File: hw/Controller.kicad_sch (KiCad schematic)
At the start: 44 parts, among them J201 Conn_01x08, J202 Molex-105017-0001, J203 Conn_01x03, J204 Conn_01x02, J205 Conn_01x02, J206 Conn_01x02, J207 Conn_01x02, P201 Current-Probe, Q201 DTC114EE, U201 STM32F401XX-LQFP64, U202 TLV62150A, X201 Mounting-Hole-M3, X202 Mounting-Hole-M3, X203 Mounting-Hole-M3, X204 Mounting-Hole-M3, Y201 MCSJK-7I-8.00-18-30-60-B-30

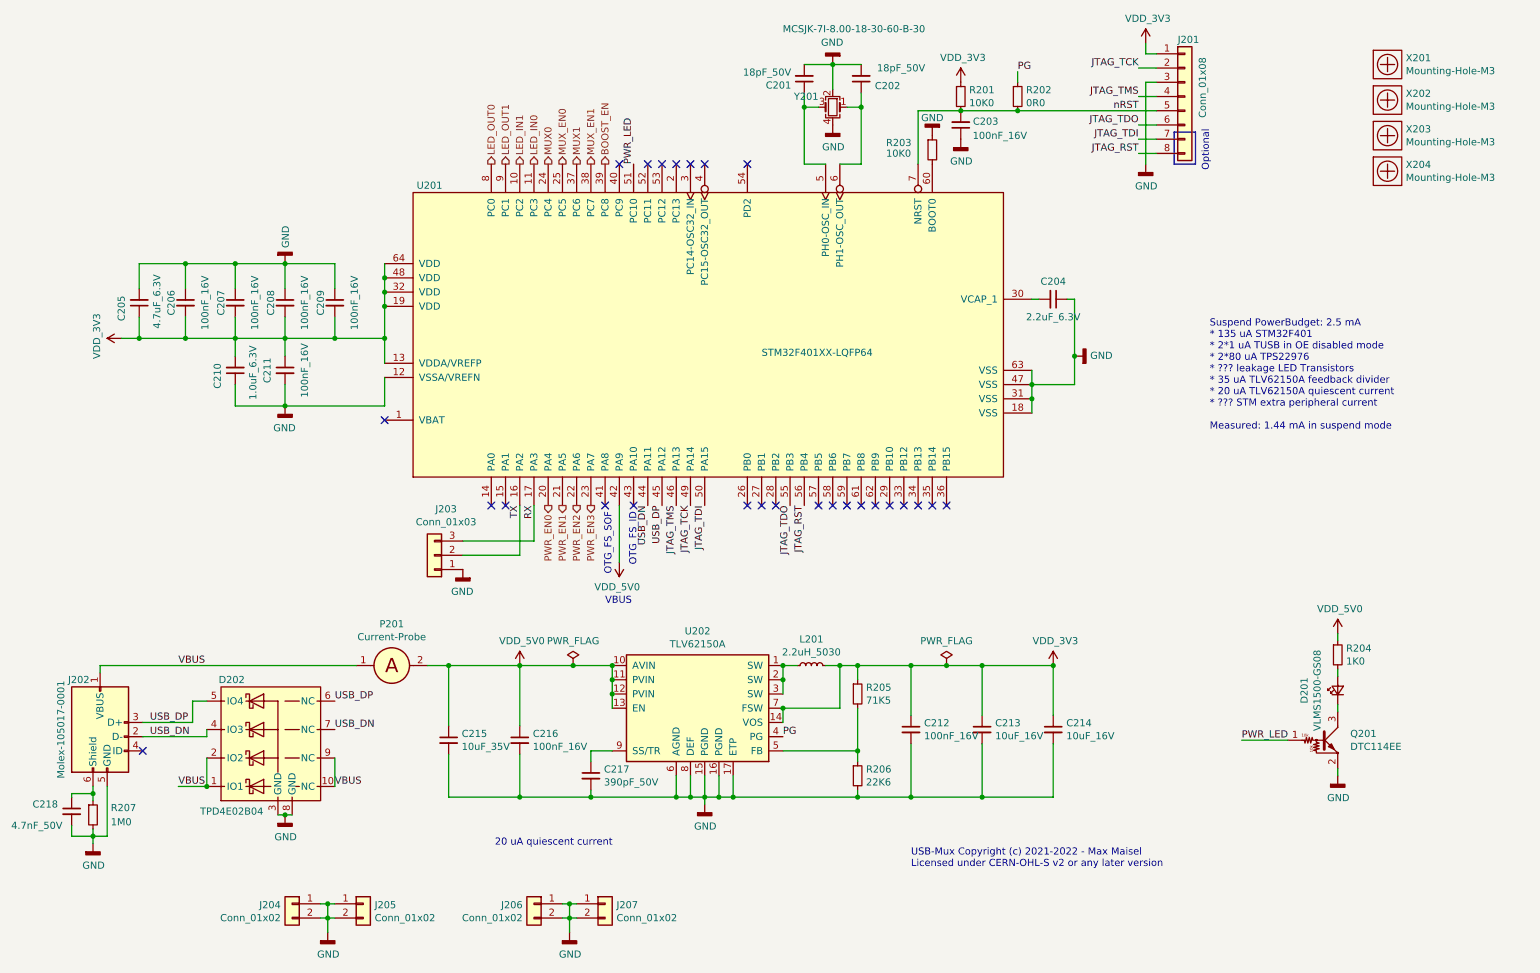
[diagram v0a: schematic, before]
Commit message: Cleanup Library
Remove unused ESD diode component and consistently name resistors X.XR.
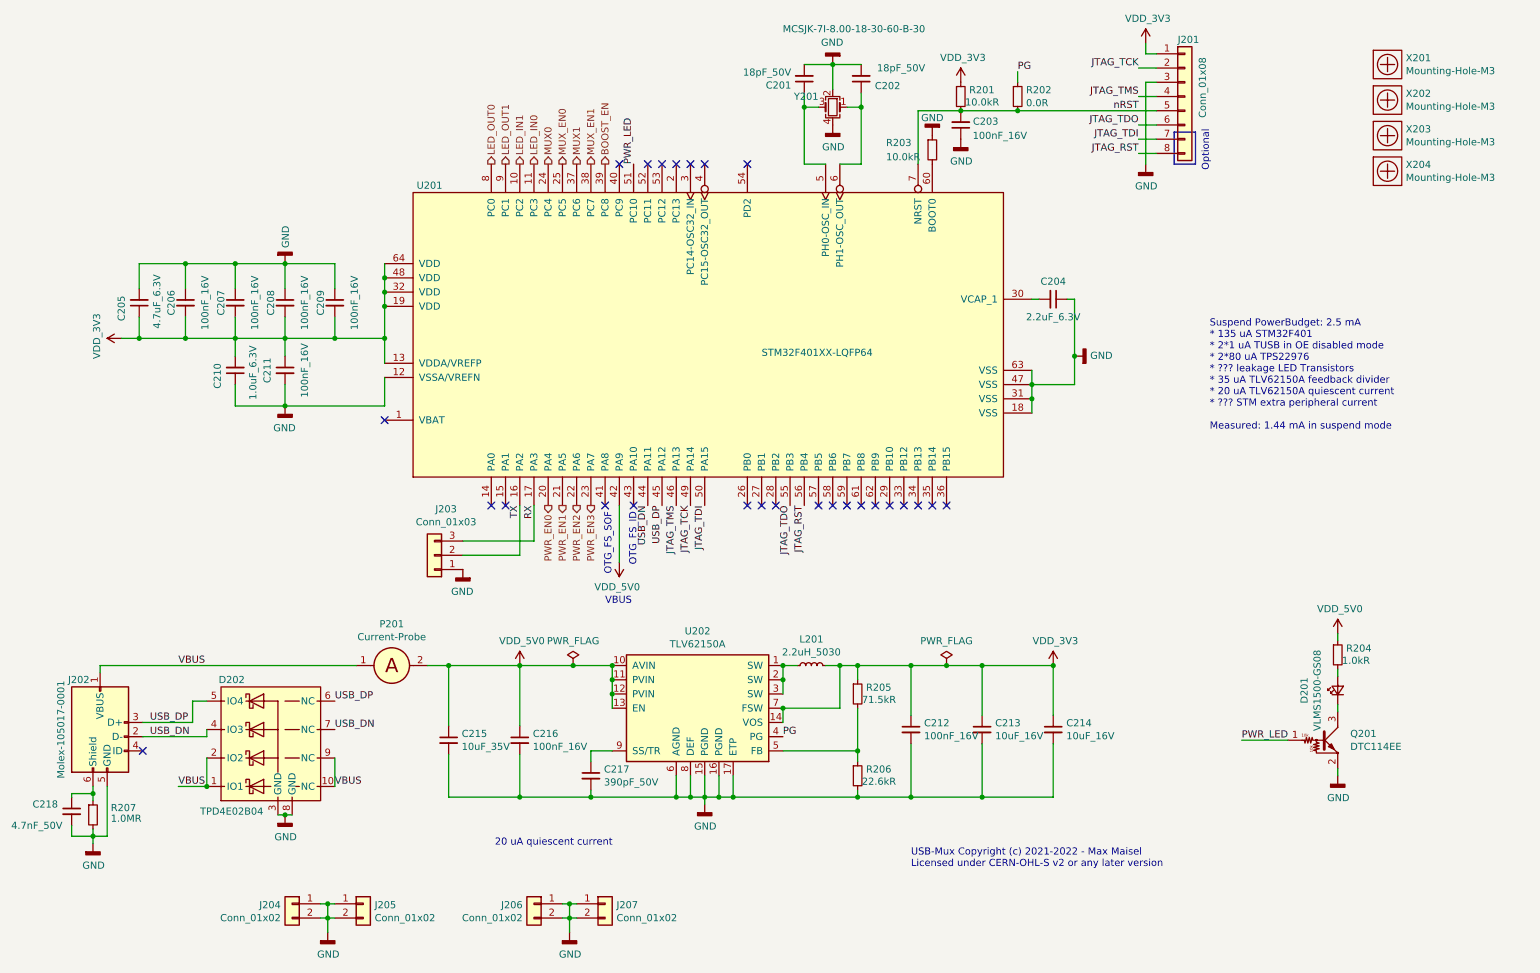
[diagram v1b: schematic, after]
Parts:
- R201, R203: value 10K0 -> 10.0kR; symbol USB-Mux:10K0 -> USB-Mux:10.0kR
- R202: value 0R0 -> 0.0R; symbol USB-Mux:0R0 -> USB-Mux:0.0R
- R204: value 1K0 -> 1.0kR; symbol USB-Mux:1K0 -> USB-Mux:1.0kR
- R205: value 71K5 -> 71.5kR; symbol USB-Mux:71K5 -> USB-Mux:71.5kR
- R206: value 22K6 -> 22.6kR; symbol USB-Mux:22K6 -> USB-Mux:22.6kR
- R207: value 1M0 -> 1.0MR; symbol USB-Mux:1M0 -> USB-Mux:1.0MR
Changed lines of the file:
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@@
     (pin "2")
   )
-  (symbol (lib_id "USB-Mux:10K0") (at 186.69 33.655 0) (unit 1)
+  (symbol (lib_id "USB-Mux:10.0kR") (at 186.69 33.655 0) (unit 1)
     (in_bom yes) (on_board yes)
     (property "Reference" "R201" (id 0) (at 188.1886 32.4866 0)
       (effects (font (size 1.27 1.27)) (justify left))
     )
-    (property "Value" "10K0" (id 1) (at 188.1886 34.798 0)
+    (property "Value" "10.0kR" (id 1) (at 187.452 34.671 0)
       (effects (font (size 1.27 1.27)) (justify left))
     )
@@
     (pin "2")
   )
-  (symbol (lib_id "USB-Mux:22K6") (at 168.275 154.94 0) (unit 1)
+  (symbol (lib_id "USB-Mux:22.6kR") (at 168.275 154.94 0) (unit 1)
     (in_bom yes) (on_board yes)
     (property "Reference" "R206" (id 0) (at 169.7736 153.7716 0)
       (effects (font (size 1.27 1.27)) (justify left))
     )
-    (property "Value" "22K6" (id 1) (at 169.7736 156.083 0)
+    (property "Value" "22.6kR" (id 1) (at 169.037 155.956 0)
       (effects (font (size 1.27 1.27)) (justify left))
     )
@@
     (pin "1")
   )
-  (symbol (lib_id "USB-Mux:71K5") (at 168.275 140.335 0) (unit 1)
+  (symbol (lib_id "USB-Mux:71.5kR") (at 168.275 140.335 0) (unit 1)
     (in_bom yes) (on_board yes)
     (property "Reference" "R205" (id 0) (at 169.7736 139.1666 0)
       (effects (font (size 1.27 1.27)) (justify left))
     )
-    (property "Value" "71K5" (id 1) (at 169.7736 141.478 0)
+    (property "Value" "71.5kR" (id 1) (at 169.037 141.351 0)
       (effects (font (size 1.27 1.27)) (justify left))
     )
@@
     (pin "2")
   )
-  (symbol (lib_id "USB-Mux:0R0") (at 196.85 33.655 0) (unit 1)
+  (symbol (lib_id "USB-Mux:0.0R") (at 196.85 33.655 0) (unit 1)
     (in_bom yes) (on_board yes)
     (property "Reference" "R202" (id 0) (at 198.3486 32.4866 0)
       (effects (font (size 1.27 1.27)) (justify left))
     )
-    (property "Value" "0R0" (id 1) (at 198.3486 34.798 0)
+    (property "Value" "0.0R" (id 1) (at 198.3486 34.798 0)
       (effects (font (size 1.27 1.27)) (justify left))
     )
@@
     (pin "1")
   )
-  (symbol (lib_id "USB-Mux:10K0") (at 181.61 43.18 0) (unit 1)
+  (symbol (lib_id "USB-Mux:10.0kR") (at 181.61 43.18 0) (unit 1)
     (in_bom yes) (on_board yes)
     (property "Reference" "R203" (id 0) (at 173.355 41.91 0)
       (effects (font (size 1.27 1.27)) (justify left))
     )
-    (property "Value" "10K0" (id 1) (at 173.355 43.815 0)
+    (property "Value" "10.0kR" (id 1) (at 173.355 44.45 0)
       (effects (font (size 1.27 1.27)) (justify left))
     )
@@
     (pin "2")
   )
-  (symbol (lib_id "USB-Mux:1M0") (at 31.75 161.925 0) (unit 1)
+  (symbol (lib_id "USB-Mux:1.0MR") (at 31.75 161.925 0) (unit 1)
     (in_bom yes) (on_board yes)
     (property "Reference" "R207" (id 0) (at 34.925 160.655 0)
       (effects (font (size 1.27 1.27)) (justify left))
     )
-    (property "Value" "1M0" (id 1) (at 34.925 163.195 0)
+    (property "Value" "1.0MR" (id 1) (at 34.925 162.56 0)
       (effects (font (size 1.27 1.27)) (justify left))
     )
@@
     (pin "3")
   )
-  (symbol (lib_id "USB-Mux:1K0") (at 254 133.35 0) (unit 1)
+  (symbol (lib_id "USB-Mux:1.0kR") (at 254 133.35 0) (unit 1)
     (in_bom yes) (on_board yes)
     (property "Reference" "R204" (id 0) (at 255.4986 132.1816 0)
       (effects (font (size 1.27 1.27)) (justify left))
     )
-    (property "Value" "1K0" (id 1) (at 255.4986 134.493 0)
-      (effects (font (size 1.27 1.27)) (justify left))
-    )
+    (property "Value" "1.0kR" (id 1) (at 254.762 134.366 0)
+      (effects (font (size 1.27 1.27)) (justify left))
+    )
